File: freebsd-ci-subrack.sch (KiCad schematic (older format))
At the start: 22 parts

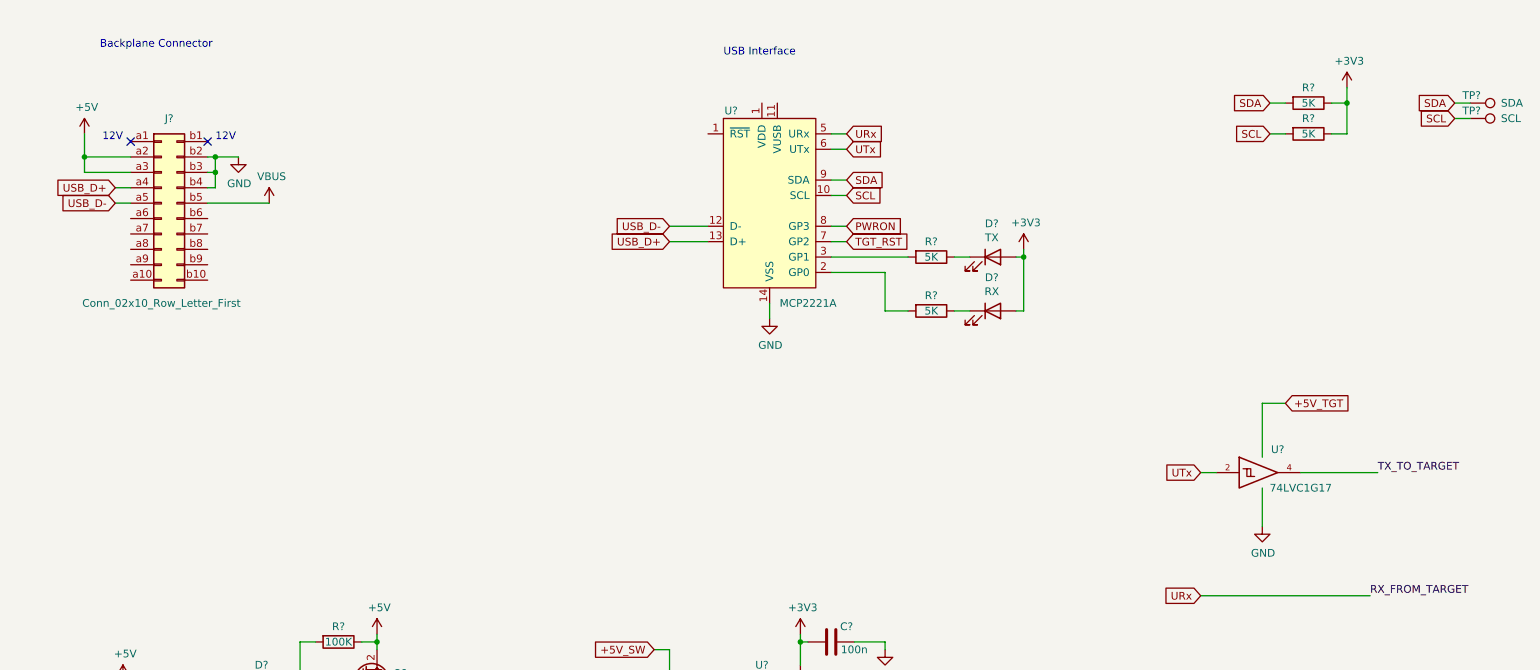
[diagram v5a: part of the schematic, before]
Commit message: Use '125 buffer
RPi UARTs are 3V3 only, so use a tri-state buffer with OE driven
by power control.  Need to check 74LV1T125 or 74LVC1G125.

Also start adding power supply components
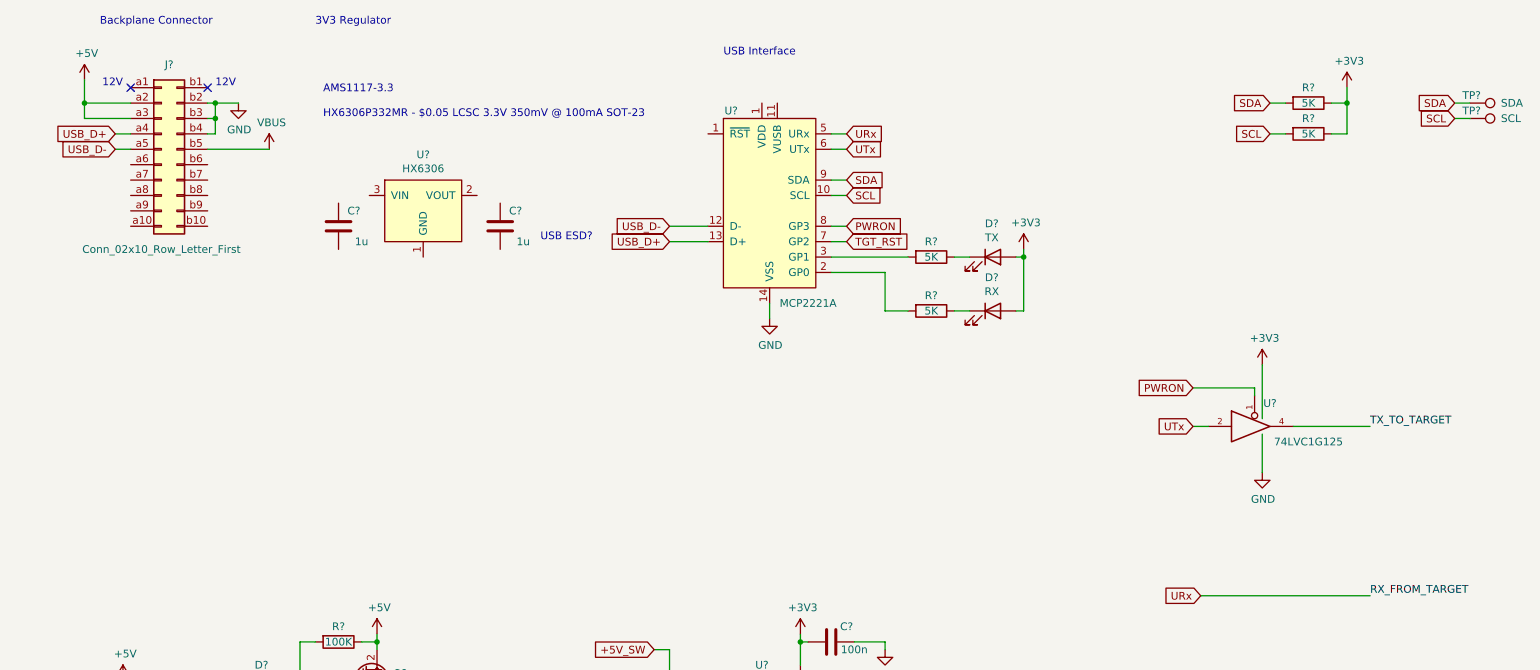
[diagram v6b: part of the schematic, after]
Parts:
- removed U?: 74LVC1G17, symbol 74xGxx:74LVC1G17
- added C? (x2): 1u, symbol Device:C
- added U?: HX6306, symbol Subrack:HX6306
- added U?: 74LVC1G125, symbol 74xGxx:74LVC1G125
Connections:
- net +3V3: now also U?.5 (VCC)
- net GND: now also U?.3 (GND)
- net PWRON: now also U?.1
- net TX_TO_TARGET: now also U?.4
- net UTx: now also U?.2
- net VCC renamed +5V_TGT
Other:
- note added: "3V3 Regulator"
- note added: "AMS1117-3.3\n\nHX6306P332MR - $0.05 LCSC 3.3V 350mV @ 100mA SOT-23"
- note added: "USB ESD?"
- moved on the sheet: J?
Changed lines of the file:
@@
 L Connector_Generic:Conn_02x10_Row_Letter_First J?
 U 1 1 60983C54
-P 1550 1800
-F 0 "J?" H 1600 2350 50  0000 C CNN
-F 1 "Conn_02x10_Row_Letter_First" H 1550 1150 50  0000 C CNN
-F 2 "" H 1550 1800 50  0001 C CNN
-F 3 "~" H 1550 1800 50  0001 C CNN
-	1    1550 1800
+P 1550 1450
+F 0 "J?" H 1600 2000 50  0000 C CNN
+F 1 "Conn_02x10_Row_Letter_First" H 1550 800 50  0000 C CNN
+F 2 "" H 1550 1450 50  0001 C CNN
+F 3 "~" H 1550 1450 50  0001 C CNN
+	1    1550 1450
 	1    0    0    -1
 $EndComp
@@
 L power:+5V #PWR?
 U 1 1 60986CBB
-P 1050 1350
-F 0 "#PWR?" H 1050 1200 50  0001 C CNN
-F 1 "+5V" H 1065 1523 50  0000 C CNN
-F 2 "" H 1050 1350 50  0001 C CNN
-F 3 "" H 1050 1350 50  0001 C CNN
-	1    1050 1350
-	1    0    0    -1
-$EndComp
-Wire Wire Line
-	1050 1350 1050 1500
-Wire Wire Line
-	1050 1600 1350 1600
-Wire Wire Line
-	1050 1500 1350 1500
-Connection ~ 1050 1500
-Wire Wire Line
-	1050 1500 1050 1600
-Text GLabel 1250 1700 0    50   Input ~ 0
+P 1050 1000
+F 0 "#PWR?" H 1050 850 50  0001 C CNN
+F 1 "+5V" H 1065 1173 50  0000 C CNN
+F 2 "" H 1050 1000 50  0001 C CNN
+F 3 "" H 1050 1000 50  0001 C CNN
+	1    1050 1000
+	1    0    0    -1
+$EndComp
+Wire Wire Line
+	1050 1000 1050 1150
+Wire Wire Line
+	1050 1250 1350 1250
+Wire Wire Line
+	1050 1150 1350 1150
+Connection ~ 1050 1150
+Wire Wire Line
+	1050 1150 1050 1250
+Text GLabel 1250 1350 0    50   Input ~ 0
 USB_D+
 Wire Wire Line
-	1250 1700 1350 1700
-Text GLabel 1250 1800 0    50   Input ~ 0
+	1250 1350 1350 1350
+Text GLabel 1250 1450 0    50   Input ~ 0
 USB_D-
 Wire Wire Line
-	1250 1800 1350 1800
+	1250 1450 1350 1450
 $Comp
 L power:VBUS #PWR?
 U 1 1 60987B29
-P 2250 1800
-F 0 "#PWR?" H 2250 1650 50  0001 C CNN
-F 1 "VBUS" H 2265 1973 50  0000 C CNN
-F 2 "" H 2250 1800 50  0001 C CNN
-F 3 "" H 2250 1800 50  0001 C CNN
-	1    2250 1800
-	1    0    0    -1
-$EndComp
-Wire Wire Line
-	1850 1800 2250 1800
+P 2250 1450
+F 0 "#PWR?" H 2250 1300 50  0001 C CNN
+F 1 "VBUS" H 2265 1623 50  0000 C CNN
+F 2 "" H 2250 1450 50  0001 C CNN
+F 3 "" H 2250 1450 50  0001 C CNN
+	1    2250 1450
+	1    0    0    -1
+$EndComp
+Wire Wire Line
+	1850 1450 2250 1450
 $Comp
 L power:GND #PWR?
 U 1 1 60988876
-P 2050 1500
-F 0 "#PWR?" H 2050 1250 50  0001 C CNN
-F 1 "GND" H 2055 1327 50  0000 C CNN
-F 2 "" H 2050 1500 50  0001 C CNN
-F 3 "" H 2050 1500 50  0001 C CNN
-	1    2050 1500
-	1    0    0    -1
-$EndComp
-Wire Wire Line
-	1850 1500 1900 1500
-Wire Wire Line
-	1900 1500 1900 1600
-Wire Wire Line
-	1900 1700 1850 1700
-Connection ~ 1900 1500
-Wire Wire Line
-	1900 1500 2050 1500
-Wire Wire Line
-	1850 1600 1900 1600
-Connection ~ 1900 1600
-Wire Wire Line
-	1900 1600 1900 1700
+P 2050 1150
+F 0 "#PWR?" H 2050 900 50  0001 C CNN
+F 1 "GND" H 2055 977 50  0000 C CNN
+F 2 "" H 2050 1150 50  0001 C CNN
+F 3 "" H 2050 1150 50  0001 C CNN
+	1    2050 1150
+	1    0    0    -1
+$EndComp
+Wire Wire Line
+	1850 1150 1900 1150
+Wire Wire Line
+	1900 1150 1900 1250
+Wire Wire Line
+	1900 1350 1850 1350
+Connection ~ 1900 1150
+Wire Wire Line
+	1900 1150 2050 1150
+Wire Wire Line
+	1850 1250 1900 1250
+Connection ~ 1900 1250
+Wire Wire Line
+	1900 1250 1900 1350
 $Comp
 L Subrack:MCP2221A U?
@@
 Wire Wire Line
 	2350 4900 2450 4900
-Text Notes 1150 800  0    50   ~ 0
+Text Notes 1150 650  0    50   ~ 0
 Backplane Connector
 Text Notes 5200 850  0    50   ~ 0
@@
 	1300 5500 1300 5400
 $Comp
-L 74xGxx:74LVC1G17 U?
-U 1 1 60AADB57
-P 8700 3550
-F 0 "U?" H 8800 3700 50  0000 C CNN
-F 1 "74LVC1G17" H 8950 3450 50  0000 C CNN
-F 2 "" H 8700 3550 50  0001 C CNN
-F 3 "http://www.ti.com/lit/sg/scyt129e/scyt129e.pdf" H 8700 3550 50  0001 C CNN
-	1    8700 3550
-	1    0    0    -1
-$EndComp
-Text GLabel 8850 3100 2    50   Input ~ 0
-+5V_TGT
-Wire Wire Line
-	8700 3450 8700 3100
-Wire Wire Line
-	8700 3100 8850 3100
-$Comp
 L power:GND #PWR?
 U 1 1 60AB1679
-P 8700 3900
-F 0 "#PWR?" H 8700 3650 50  0001 C CNN
-F 1 "GND" H 8705 3727 50  0000 C CNN
-F 2 "" H 8700 3900 50  0001 C CNN
-F 3 "" H 8700 3900 50  0001 C CNN
-	1    8700 3900
-	1    0    0    -1
-$EndComp
-Wire Wire Line
-	8700 3650 8700 3900
+P 8700 3550
+F 0 "#PWR?" H 8700 3300 50  0001 C CNN
+F 1 "GND" H 8705 3377 50  0000 C CNN
+F 2 "" H 8700 3550 50  0001 C CNN
+F 3 "" H 8700 3550 50  0001 C CNN
+	1    8700 3550
+	1    0    0    -1
+$EndComp
+Wire Wire Line
+	8700 3300 8700 3550
 Text GLabel 6000 1350 2    50   Input ~ 0
 URx
@@
 Wire Wire Line
 	5900 1350 6000 1350
-Text GLabel 8300 3550 0    50   Input ~ 0
+Text GLabel 8250 3250 0    50   Input ~ 0
 UTx
-Wire Wire Line
-	8300 3550 8400 3550
-Text Label 9450 3550 0    50   ~ 0
+Text Label 9400 3250 0    50   ~ 0
 TX_TO_TARGET
 Wire Wire Line
-	8950 3550 9450 3550
+	8900 3250 9400 3250
 Text GLabel 8300 4350 0    50   Input ~ 0
 URx
@@
 Wire Wire Line
 	5900 2050 6000 2050
-NoConn ~ 1350 1400
-NoConn ~ 1850 1400
-Text Notes 1900 1400 0    50   ~ 0
+NoConn ~ 1350 1050
+NoConn ~ 1850 1050
+Text Notes 1900 1050 0    50   ~ 0
 12V
-Text Notes 1300 1400 2    50   ~ 0
+Text Notes 1300 1050 2    50   ~ 0
 12V
+Text Notes 2550 650  0    50   ~ 0
+3V3 Regulator
+Text Notes 2600 1250 0    50   ~ 0
+AMS1117-3.3\n\nHX6306P332MR - $0.05 LCSC 3.3V 350mV @ 100mA SOT-23
+Text Notes 4350 2050 2    50   ~ 0
+USB ESD?
+$Comp
+L Subrack:HX6306 U?
+U 1 1 609B48E9
+P 3250 1750
+F 0 "U?" H 3250 2015 50  0000 C CNN
+F 1 "HX6306" H 3250 1924 50  0000 C CNN
+F 2 "" H 3250 1750 50  0001 C CNN
+F 3 "" H 3250 1750 50  0001 C CNN
+	1    3250 1750
+	1    0    0    -1
+$EndComp
+$Comp
+L Device:C C?
+U 1 1 609B519E
+P 2700 1950
+F 0 "C?" H 2600 1850 50  0000 C CNN
+F 1 "1u" H 2550 2050 50  0000 C CNN
+F 2 "" H 2738 1800 50  0001 C CNN
+F 3 "~" H 2700 1950 50  0001 C CNN
+	1    2700 1950
+	-1   0    0    1
+$EndComp
+$Comp
+L Device:C C?
+U 1 1 609B69E4
+P 3750 1950
+F 0 "C?" H 3650 1850 50  0000 C CNN
+F 1 "1u" H 3600 2050 50  0000 C CNN
+F 2 "" H 3788 1800 50  0001 C CNN
+F 3 "~" H 3750 1950 50  0001 C CNN
+	1    3750 1950
+	-1   0    0    1
+$EndComp
+$Comp
+L 74xGxx:74LVC1G125 U?
+U 1 1 609BA642
+P 8650 3250
+F 0 "U?" H 8750 3400 50  0000 C CNN
+F 1 "74LVC1G125" H 9000 3150 50  0000 C CNN
+F 2 "" H 8650 3250 50  0001 C CNN
+F 3 "http://www.ti.com/lit/sg/scyt129e/scyt129e.pdf" H 8650 3250 50  0001 C CNN
+	1    8650 3250
+	1    0    0    -1
+$EndComp
+Wire Wire Line
+	8250 3250 8350 3250
+$Comp
+L power:+3V3 #PWR?
+U 1 1 609C5A80
+P 8700 2850
+F 0 "#PWR?" H 8700 2700 50  0001 C CNN
+F 1 "+3V3" H 8715 3023 50  0000 C CNN
+F 2 "" H 8700 2850 50  0001 C CNN
+F 3 "" H 8700 2850 50  0001 C CNN
+	1    8700 2850
+	1    0    0    -1
+$EndComp
+Wire Wire Line
+	8700 3200 8700 2850
+Text GLabel 8250 3000 0    50   Input ~ 0
+PWRON
+Wire Wire Line
+	8250 3000 8650 3000
+Wire Wire Line
+	8650 3000 8650 3050
 $EndSCHEMATC

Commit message: Snapshot after choosing most parts
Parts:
- removed D?: TGT_PWR, symbol Device:LED
- removed D?: D, symbol Device:D
- removed R? (x4): 5K, symbol Device:R
- removed R?: 100K, symbol Device:R
- removed R?: 10K, symbol Device:R
- removed U?: 74LVC1G125, symbol 74xGxx:74LVC1G125
- removed U?: SN74LVC1G14DBV, Package_TO_SOT_SMD:SOT-23-5, symbol 74xGxx:SN74LVC1G14DBV
- added C? (x4): 100n, symbol Device:C
- added D? (x4): +5V, symbol Device:LED
- added D? (x2): SS14, Diode_SMD:D_SMA, symbol Device:D
- added D?: LL4148, Diode_SMD:D_MiniMELF, symbol Diode:LL4148
- added D?: RX, symbol Device:LED
- added J?: Conn_02x05_Odd_Even, symbol Connector_Generic:Conn_02x05_Odd_Even
- added JP?: SolderJumper_2_Open, symbol Jumper:SolderJumper_2_Open
- added JP?: SolderJumper_2_Bridged, symbol Jumper:SolderJumper_2_Bridged
- added Q?: 2N7002, Package_TO_SOT_SMD:SOT-23, symbol Transistor_FET:2N7002
- added R?: 100K, symbol Device:R
- added R?: 10K, symbol Device:R
- added R? (x8): 5K, Resistor_SMD:R_0603_1608Metric, symbol Device:R
- added R? (x2): 100R, Resistor_SMD:R_0603_1608Metric, symbol Device:R
- added R?: 100K, Resistor_SMD:R_0603_1608Metric, symbol Device:R
- added R?: 10K, Resistor_SMD:R_0603_1608Metric, symbol Device:R
- added R?: DNP, Resistor_SMD:R_0603_1608Metric, symbol Device:R
- added SW?: SW_MEC_5E, symbol Switch:SW_MEC_5E
- added TP?: TGT_RST, symbol Connector:TestPoint
- added TP?: TEMP_D+, symbol Connector:TestPoint
- added TP?: TEMP_D-, symbol Connector:TestPoint
- added U?: USBLC6-2SC6, Package_TO_SOT_SMD:SOT-23-6, symbol Power_Protection:USBLC6-2SC6
- added U?: 74AHCT1G04, symbol 74xGxx:74AHCT1G04
- added U?: 74LVC1G126, symbol 74xGxx:74LVC1G126
- added U?: TMP411, symbol Sensor_Temperature:TMP411
- R?: value R -> R010 1% 1206; footprint (none) -> Resistor_SMD:R_1206_3216Metric
- R?: footprint (none) -> Resistor_SMD:R_0603_1608Metric
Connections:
- net +5V is gone; now on net +3V3: J?.a2 (Pin_a2), J?.a3 (Pin_a3), Q?.2 (D)
- net +3V3: now also C?.2, U?.1 (~RST), U?.11 (VUSB), U?.2 (VOUT), C?.1, C?.2, C?.2, D?.2 (A), D?.2 (A), JP?.1 (A), R?.1, R?.2, R?.2, R?.2, R?.2, R?.2, U?.1 (V+), U?.5 (VCC), U?.5 (VCC)
- net +5V_SW: now also R?.2
- net GND: now also C?.1, C?.1, U?.1 (GND), C?.1, C?.1, C?.1, C?.2, D?.1 (K), D?.1 (K), D?.1 (K), D?.1 (K), J?.6 (Pin_6), J?.9 (Pin_9), Q?.2 (S), SW?.3 (K), SW?.4 (A), U?.2 (GND), U?.3 (GND), U?.3 (GND), U?.5 (GND)
- net PWRON: now also U?.1, U?.2
- net SCL: now also R?.1, U?.8 (SCL)
- net SDA: now also R?.1, U?.7 (SDA)
- net TGT_RST: now also Q?.3 (D), R?.1, R?.2, SW?.1, SW?.2, TP?.1; no longer U?.7 (GP2)
- net URx: now also R?.2
- net USB_D+: now also U?.1 (I/O1); no longer J?.a4 (Pin_a4)
- net USB_D-: now also U?.3 (I/O2); no longer J?.a5 (Pin_a5)
- net UTx: now also R?.2, U?.2
- net VBUS: now also C?.2, D?.2 (A), JP?.1 (A), R?.2, U?.5 (VBUS)
- net ~RXLED: now reaches U?.2 (GP0)
- net ~RXLED: now also R?.2
- net ~TXLED: now reaches R?.2, U?.3 (GP1)
- net at D?.1 (K): now also R?.1
- net at U?.3 (VIN): now also C?.2, D?.1 (K), D?.1 (K), JP?.2 (B)
- net at C?.2, Q?.1 (G): now also D?.1 (K), R?.1, R?.2
- net +5V_TGT renamed TGT_+5V
- net TGT_+5V: now also J?.2 (Pin_2), J?.4 (Pin_4)
- new net: J?.a4 (Pin_a4), U?.6 (I/O1)
- new net: J?.a5 (Pin_a5), U?.4 (I/O2)
- new net: JP?.2 (B), U?.1 (~RST)
- new net: Q?.1 (G), R?.1
- new net: D?.2 (A), R?.2, U?.4
- new net: D?.2 (A), R?.1 (x4)
- new net: R?.2, U?.4
- new net: D?.1 (K), R?.1
- new net: TP?.1, U?.2 (D+)
- new net: TP?.1, U?.3 (D-)
- new net RESET: R?.2, U?.7 (GP2)
- new net TGT_RX: J?.10 (Pin_10), R?.1, R?.1
- new net TGT_TX: J?.8 (Pin_8), R?.1
- no-connect marks 2 -> 18
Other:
- note added: "3V3"
- note added: "Check if MCP2221A has built-in pullups\n(if so leave these as DNP)"
- note added: "ETH"
- note added: "Energy Monitor"
- note added: "HX6306P332MR\n3.3V 350mV @ 100mA SOT-23\n$0.05 LCSC \n"
- note added: "I2C Pullups"
- note added: "Other options:\nMCP28243\nLM75"
- note added: "RSVD"
- note added: "Status LEDs"
- note added: "Target Connector"
- note added: "Target Power Control"
- note added: "UART Connections"
- note added: "XXX No reset on RPi GPIO"
- note removed: "AMS1117-3.3\n\nHX6306P332MR - $0.05 LCSC 3.3V 350mV @ 100mA SOT-23"
- note removed: "USB ESD?"
- moved on the sheet: C?, D?, J?, Q?, R?, TP?, U?

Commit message: Additional temperature sensors
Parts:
- removed Q?: Q_PMOS_GDS, symbol Device:Q_PMOS_GDS
- added C?: 1u, symbol Device:C
- added C? (x2): 100n, symbol Device:C
- added Q?: PJM3415PSA, symbol Device:Q_PMOS_GSD
- added TP? (x4): TP, symbol Connector:TestPoint
- added U?: LM75B, symbol Sensor_Temperature:LM75B
- added U?: MCP98243, symbol Subrack:MCP98243
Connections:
- net +3V3: now also C?.2, C?.2, C?.2, Q?.2 (S), U?.8 (+Vs), U?.8 (VDD)
- net +5V_SW: now also Q?.3 (D)
- net GND: now also C?.1, C?.1, C?.1, U?.4 (GND), U?.4 (GND)
- net SCL: now also U?.2 (SCL), U?.6 (SCL)
- net SDA: now also U?.1 (SDA), U?.5 (SDA)
- net at C?.2, D?.1 (K), R?.1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: now also Q?.1 (G)
- net at U?.4 (~TERM): now also TP?.1
- net at U?.6 (~ALERT): now also TP?.1
- new net: TP?.1, U?.3 (O.S.)
- new net: TP?.1, U?.7 (EVENT)
- no-connect marks 18 -> 16
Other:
- note added: "- 98243 for compatibity with L41 design\n- TMP411 for remote sensor\n- LM75B for availability"
- note added: "Cover All Bases Temperature Sensors"
- note added: "Open Drain Reset Driver"
- note added: "PJM3415PSA $0.43 P-Channel -20V 4A 1V @ 250uA 50mΩ @ 4A,4.5V 1.5W SOT-23 MOSFET RoHS\n\n"
- note removed: "Other options:\nMCP28243\nLM75"
- moved on the sheet: C?, D?, J?, Q?, R?, SW?, TP?, U?
